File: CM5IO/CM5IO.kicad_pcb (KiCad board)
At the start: 4 copper layers, 59.7 x 78 mm, 64 parts, among them J1 POWER TERMINAL, J11 USB_C_Receptacle_USB2.0, J12 USB3_A, J14 JST_SHBM04B-SRSS-TB, J16 Conn_01x22_Female, J2 Conn_02x06_Odd_Even, J22 46765-1301, J4 J_PSU_EN, J5 Conn_01x22_Female, J7 Micro_SD_Card_Det, J8 THD-20-R, SW1 Right angle Tact button, U12 RT9742SNGV, U18 RT9742GGJ5, U6 AP22653W6

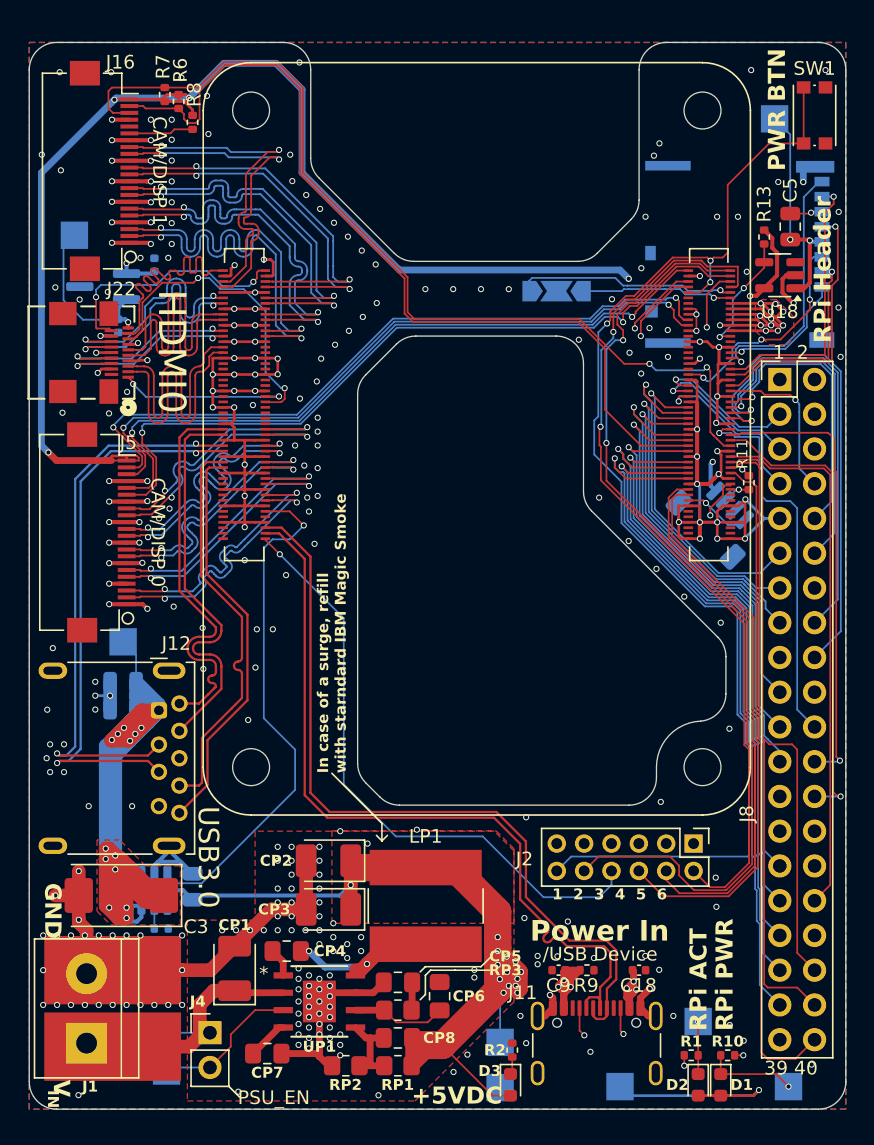
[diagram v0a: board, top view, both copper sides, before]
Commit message: DRC fixes after changing via size. fixed too small cap in PSU.
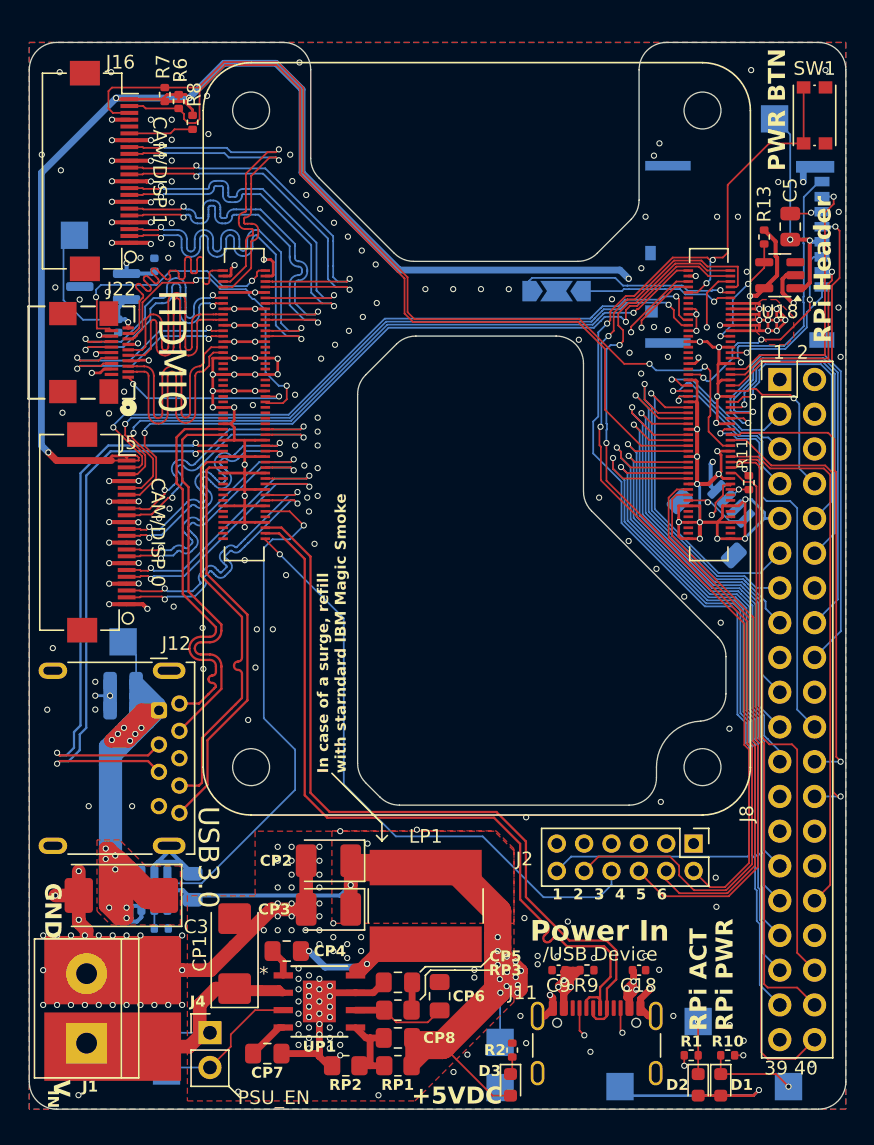
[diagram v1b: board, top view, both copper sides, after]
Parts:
- CP1: footprint Capacitor_Tantalum_SMD:CP_EIA-3528-21_Kemet-B_HandSolder -> Capacitor_Tantalum_SMD:CP_EIA-6032-28_Kemet-C_HandSolder
- moved CP1 1.08 mm to (161.3, 135.1)
- moved J14 0.13 mm to (196.7, 103.2)
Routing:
- net /VIN: track 21.5 -> 25.7 mm
- net /CM5_HighSpeed/HDMI0_SCL: track 20.2 -> 22.0 mm
- net /CM5_GPIO ( Ethernet, GPIO, SDCARD)/GPIO22: track 24.9 -> 26.7 mm
- net /+5v: track 317.7 -> 318.8 mm, vias 34 -> 32
- net GND: track 788.2 -> 787.4 mm, vias 303 -> 293
- net /CM5_GPIO ( Ethernet, GPIO, SDCARD)/GPIO2: track 10.6 -> 11.3 mm
- net /CM5_GPIO ( Ethernet, GPIO, SDCARD)/CAM_GPIO1: track 52.5 -> 51.8 mm
- net /CM5_HighSpeed/HDMI0_CEC: track 22.8 -> 23.4 mm
- net /CM5_GPIO ( Ethernet, GPIO, SDCARD)/CAM_GPIO0: track 56.0 -> 55.4 mm
- net /CM5_GPIO ( Ethernet, GPIO, SDCARD)/nPWR_LED: track 61.1 -> 61.6 mm

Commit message: Add PCIe connector. Fix some clearance violations.
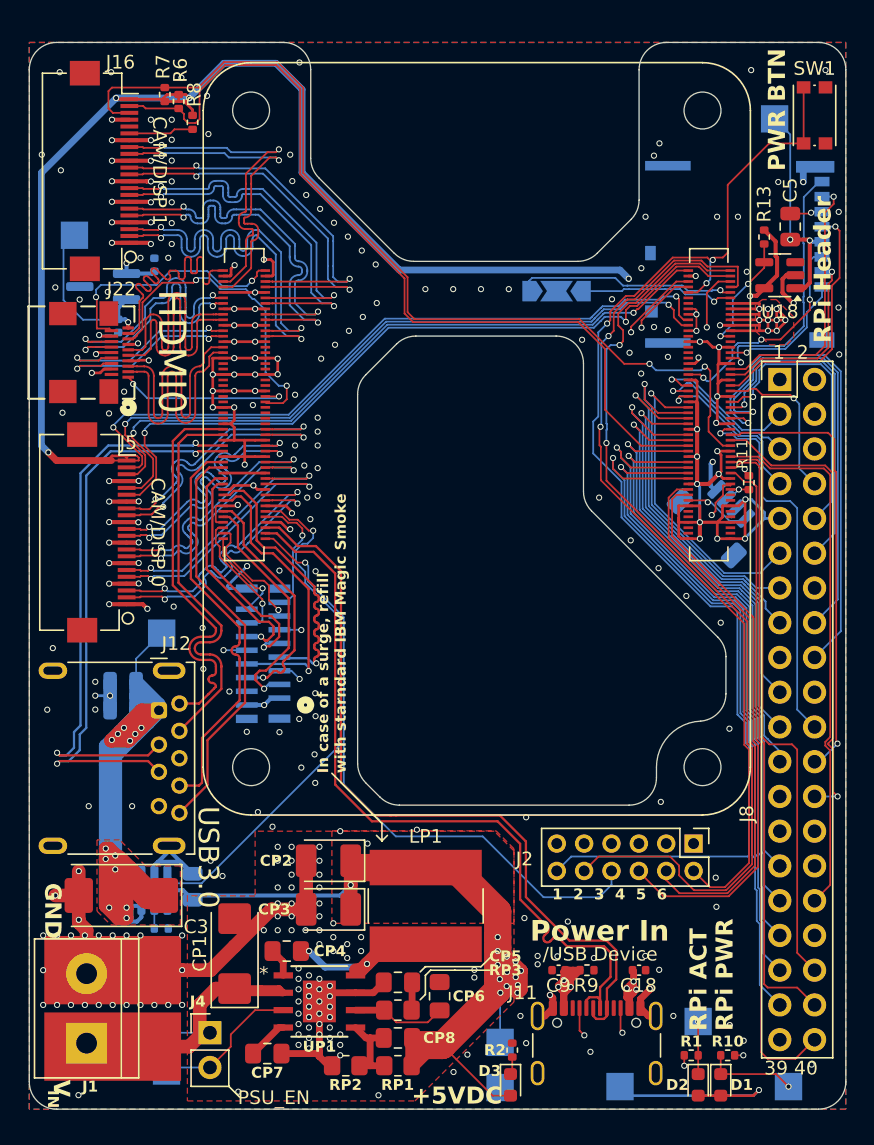
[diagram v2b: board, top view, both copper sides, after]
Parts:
- added J3: 62674-161121ALF, CM5IO:CON16_1X16_DUT_58XF_GLE, B.Cu at (164.6, 117.0)
- moved TP9 2.89 mm to (156.0, 111.7)
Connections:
- Module1 pad 102: unconnected-(Module1B-PCIe_nCLKREQ-Pad102) -> /CM5_HighSpeed/PCIE_CLKREQ_N
- Module1 pad 104: unconnected-(Module1B-PCIE_nWAKE-Pad104) -> /CM5_HighSpeed/PCIE_DET_WAKE
- Module1 pad 106: unconnected-(Module1B-PCIE_PWR_EN-Pad106) -> /CM5_HighSpeed/PCIE_PWR_EN
- Module1 pad 109: unconnected-(Module1B-PCIe_nRST-Pad109) -> /CM5_HighSpeed/PCIE_RST_B
- Module1 pad 110: unconnected-(Module1B-PCIe_CLK_P-Pad110) -> /CM5_HighSpeed/PCIE_CLK_P
- Module1 pad 112: unconnected-(Module1B-PCIe_CLK_N-Pad112) -> /CM5_HighSpeed/PCIE_CLK_N
- Module1 pad 116: unconnected-(Module1B-PCIe_RX_P-Pad116) -> /CM5_HighSpeed/PCIE_RX_P
- Module1 pad 118: unconnected-(Module1B-PCIe_RX_N-Pad118) -> /CM5_HighSpeed/PCIE_RX_N
- Module1 pad 122: unconnected-(Module1B-PCIe_TX_P-Pad122) -> /CM5_HighSpeed/PCIE_TX_P
- Module1 pad 124: unconnected-(Module1B-PCIe_TX_N-Pad124) -> /CM5_HighSpeed/PCIE_TX_N
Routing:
- net /CM5_HighSpeed/PCIE_RX_P: track 0.00 -> 21.6 mm, vias 0 -> 1
- net /CM5_HighSpeed/PCIE_RX_N: track 0.00 -> 21.5 mm, vias 0 -> 1
- net /CM5_HighSpeed/PCIE_CLK_P: track 0.00 -> 17.6 mm, vias 0 -> 1
- net /CM5_HighSpeed/PCIE_CLK_N: track 0.00 -> 17.5 mm, vias 0 -> 1
- net /CM5_HighSpeed/PCIE_TX_P: track 0.00 -> 17.0 mm, vias 0 -> 1
- net /CM5_HighSpeed/PCIE_TX_N: track 0.00 -> 17.0 mm, vias 0 -> 1
- net /CM5_HighSpeed/PCIE_PWR_EN: track 0.00 -> 9.83 mm, vias 0 -> 1
- net /CM5_HighSpeed/PCIE_RST_B: track 0.00 -> 9.44 mm, vias 0 -> 1
- net /CM5_HighSpeed/PCIE_DET_WAKE: track 0.00 -> 8.80 mm, vias 0 -> 1
- net /+5v: track 318.8 -> 326.8 mm, vias 32 -> 33
- net /CM5_HighSpeed/PCIE_CLKREQ_N: track 0.00 -> 7.12 mm, vias 0 -> 1
- net GND: track 787.4 -> 793.6 mm, vias 293 -> 304
- net /CM5_GPIO ( Ethernet, GPIO, SDCARD)/GPIO8: track 33.5 -> 32.4 mm
- net /USB2_N: track 57.8 -> 56.7 mm
- net /USB2_P: track 57.8 -> 56.7 mm
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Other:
- board text added: "Built-in AP64501 converter supplies 5V, 5A MAX. 3V3 line is supplied by RPi, 600mA MAX. Vin MAX = 40V but is limited by CP1"
- board text added: "DO NOT CONNECT USB AND Vin AT ONCE!"
- board text removed: "Built-in AP64501 converter supplies 5V, 5A MAX. 3V3 line is supplied by RPi, 600mA MAX. Vin MAX = 40V but is limited by CP1 DO NOT CONNECT USB AND Vin AT ONCE!"

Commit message: minor aesthetic changes
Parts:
- moved R7 2.08 mm to (158.2, 72.0)
- moved J11 0.27 mm to (187.8, 143.1)
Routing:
- net /+3.3v: track 199.8 -> 200.8 mm
- net /USB2_N: track 56.7 -> 57.5 mm
- net GND: track 793.6 -> 794.2 mm, vias 304 -> 309
- net /+5v: track 326.8 -> 327.1 mm, vias 33 -> 35
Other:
- board text added: "PCIe2.0 x1"
